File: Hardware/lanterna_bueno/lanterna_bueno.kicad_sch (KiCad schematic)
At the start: 52 parts, among them Q4 2SK4075, Q5 2SK4075

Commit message: building
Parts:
- removed C10, C7: (no value), symbol Device:C
- removed D6: (no value), symbol Diode:BAT54C
- removed JP1: (no value), symbol Jumper:SolderJumper_2_Open
- removed R8: (no value), symbol Device:R
- removed U4: (no value), symbol MCU_ST_STM32F1:STM32F103CBTx
- added U4: (no value), symbol MCU_ST_STM32F0:STM32F042K6Tx
- C1, C3, C6: value (none) -> 1uF; footprint (none) -> Capacitor_SMD:C_1206_3216Metric
- C11, C14: value (none) -> 10uF; footprint (none) -> Capacitor_SMD:C_1206_3216Metric
- C13: value 2.2uF -> (none); footprint Capacitor_SMD:C_1206_3216Metric -> (none)
- C2: value (none) -> 22nF; footprint (none) -> Capacitor_SMD:C_0603_1608Metric
- C4, C5: value (none) -> 1uF; footprint (none) -> Capacitor_SMD:CP_Elec_4x3
- C8, C9: value (none) -> 100nF; footprint (none) -> Capacitor_SMD:C_0603_1608Metric
- D2: value 1N5819 -> (none); footprint Diode_THT:D_DO-41_SOD81_P10.16mm_Horizontal -> (none)
- D3: value (none) -> LED
- DS1: value (none) -> OLED-128O064D; footprint (none) -> Display:OLED-128O064D
- J1: value (none) -> USB_B_Micro; footprint (none) -> Connector_USB:USB_Micro-B_Wuerth_629105150521
- Q1: value (none) -> BC807; footprint (none) -> Package_TO_SOT_SMD:SOT-23
- Q2, Q3: value (none) -> 2SK4075; footprint (none) -> Package_TO_SOT_SMD:TO-252-2
- R1: value (none) -> 100k; footprint (none) -> Resistor_SMD:R_0603_1608Metric
- R10: value (none) -> 0R4; footprint (none) -> Resistor_SMD:R_0603_1608Metric
- R11: value (none) -> 1K5; footprint (none) -> Resistor_SMD:R_0603_1608Metric
- R12: value (none) -> 0R; footprint (none) -> Resistor_SMD:R_0603_1608Metric
- R13, R2, R3, R9: value (none) -> 47K; footprint (none) -> Resistor_SMD:R_0603_1608Metric
- R14: value (none) -> 100K; footprint (none) -> Resistor_SMD:R_0603_1608Metric
- R15: value (none) -> 4K7; footprint (none) -> Resistor_SMD:R_0603_1608Metric
- R16: value (none) -> 390R; footprint (none) -> Resistor_SMD:R_0603_1608Metric
- R4, R5, R6, R7: value (none) -> 10R; footprint (none) -> Resistor_SMD:R_0603_1608Metric
- U1: value (none) -> RT9193-33; footprint (none) -> Package_TO_SOT_SMD:SOT-23-5
- U2, U3: value (none) -> IR2101; footprint (none) -> Package_SO:SOIC-8_3.9x4.9mm_P1.27mm
- U5: value (none) -> TP4056; footprint (none) -> Package_SO:Infineon_PG-DSO-8-43
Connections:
- net +3V3: now also U4.1 (VDD), U4.17 (VDDIO2), U4.5 (VDDA)
- net BAT_MON: now also U4.6 (PA0)
- net BUT_MENU: now also U4.28 (PB5)
- net BUT_MINUS: now also U4.26 (PB3)
- net BUT_PLUS: now also U4.27 (PB4)
- net GND: now also U4.16 (VSS), U4.32 (VSSA)
- net LCD_SCL: now also U4.3 (PF1)
- net LCD_SDA: now also U4.2 (PF0)
- net POWER_CMD: now also U4.29 (PB6)
- net PWM_LED_INFH: now also U4.14 (PB0)
- net PWM_LED_INFL: now also U4.15 (PB1)
- net PWM_LED_SUPH: now also U4.12 (PA6)
- net PWM_LED_SUPL: now also U4.13 (PA7)
- net at R9.2: now also U4.4 (NRST)
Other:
- moved on the sheet: R9

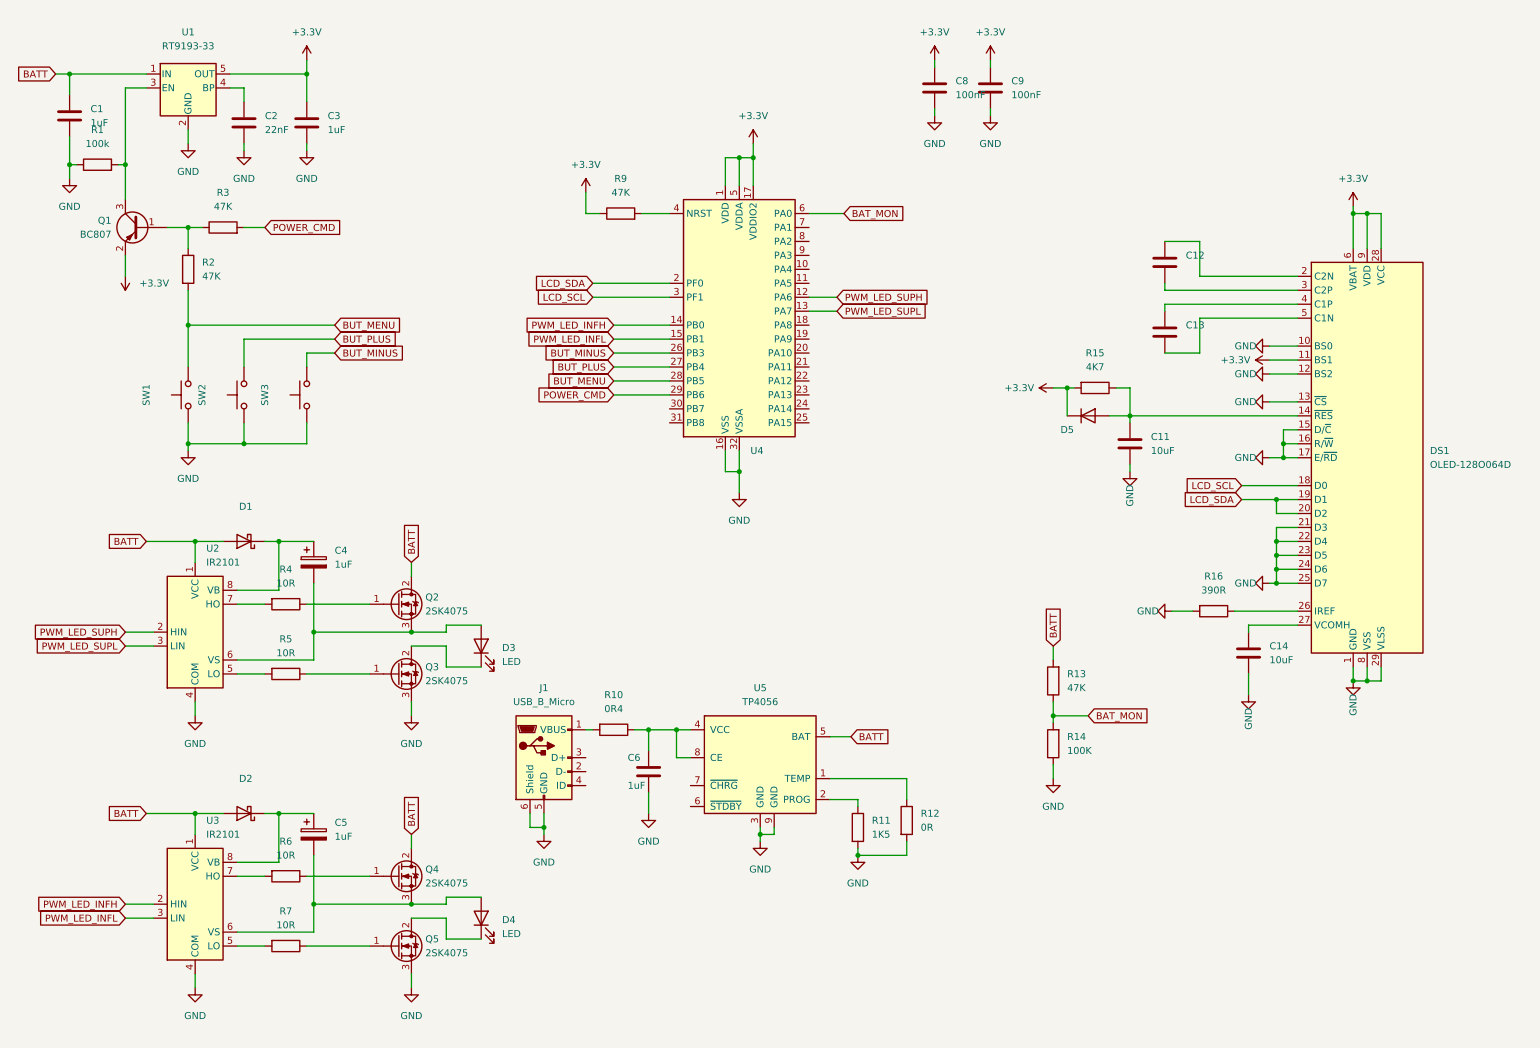
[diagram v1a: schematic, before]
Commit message: usb c
falta posicionar
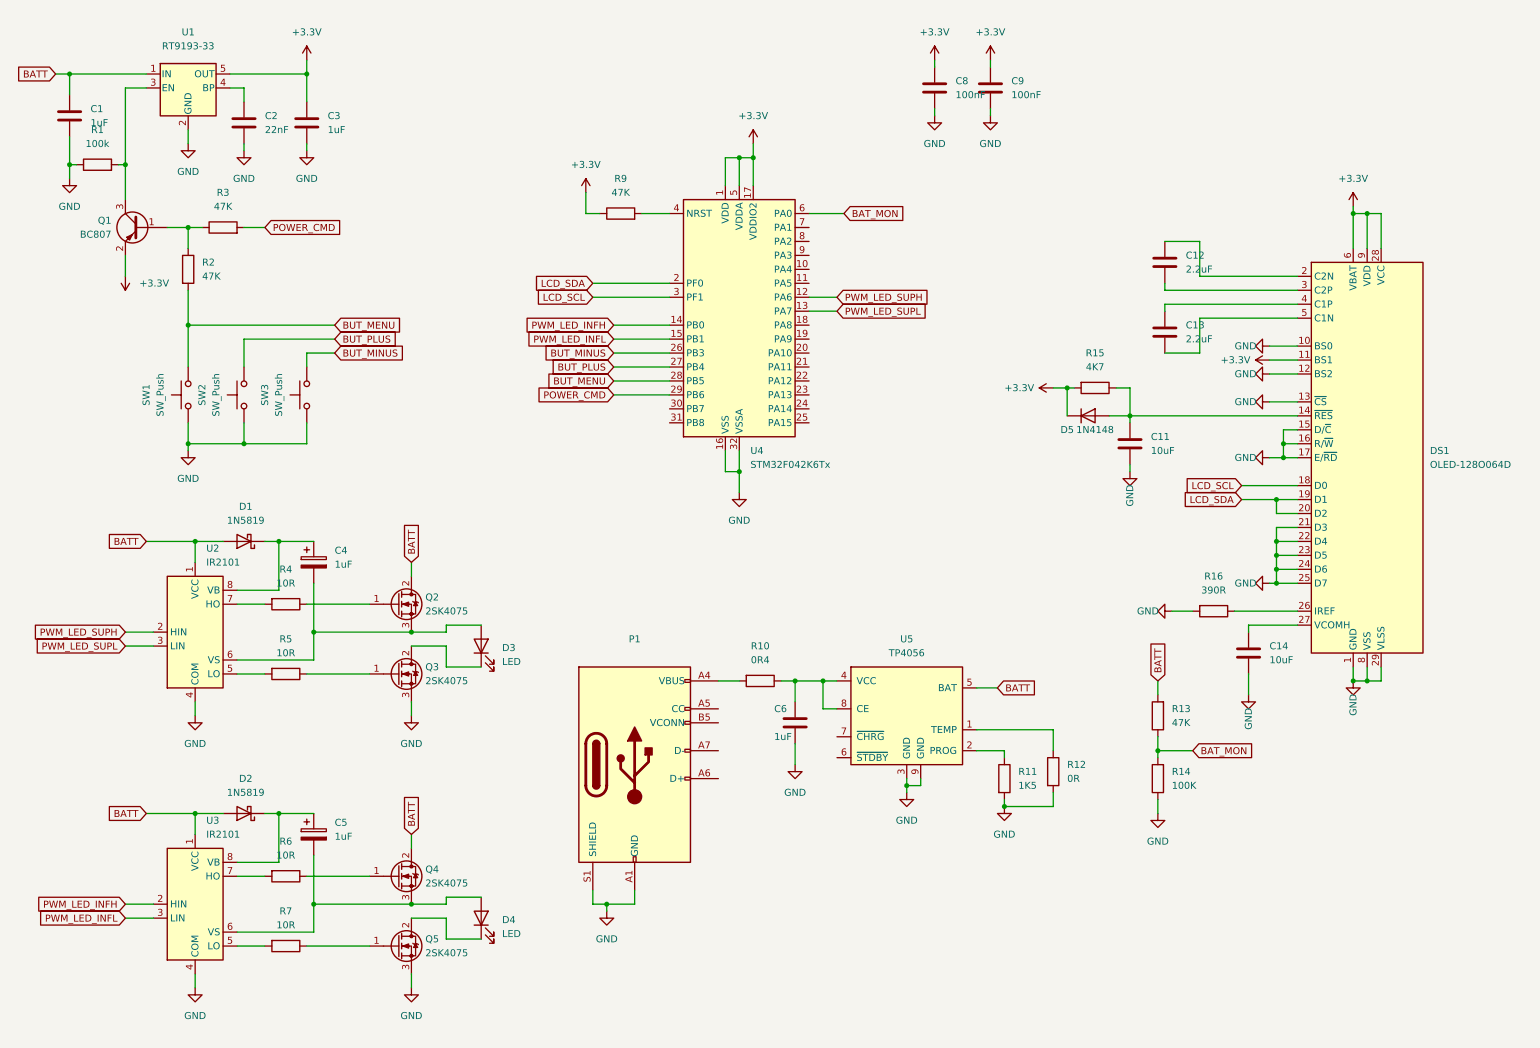
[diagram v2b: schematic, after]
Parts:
- removed J1: USB_B_Micro, Connector_USB:USB_Micro-B_Wuerth_629105150521, symbol Connector:USB_B_Micro
- added P1: (no value), symbol Connector:USB_C_Plug_USB2.0
- C12, C13: value (none) -> 2.2uF; footprint (none) -> Capacitor_SMD:C_0603_1608Metric
- D1, D2: value (none) -> 1N5819; footprint (none) -> Diode_SMD:D_SMA
- D5: value (none) -> 1N4148; footprint (none) -> Diode_SMD:D_SOD-123
- SW1, SW2, SW3: value (none) -> SW_Push; footprint (none) -> Button_Switch_SMD:SW_Push_1P1T_NO_6x6mm_H9.5mm
- U4: value (none) -> STM32F042K6Tx; footprint (none) -> Package_QFP:LQFP-32_7x7mm_P0.8mm
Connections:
- net GND: now also P1.A1 (GND), P1.A12 (GND), P1.B1 (GND), P1.B12 (GND), P1.S1 (SHIELD)
- net at R10.2: now also P1.A4 (VBUS), P1.A9 (VBUS), P1.B4 (VBUS), P1.B9 (VBUS)
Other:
- moved on the sheet: C6, R10, R11, R12, R13, R14, U5

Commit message: building pcb
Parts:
- removed D3, D4: LED, symbol Device:LED
- removed P1: (no value), symbol Connector:USB_C_Plug_USB2.0
- removed Q2, Q3, Q4, Q5: 2SK4075, Package_TO_SOT_SMD:TO-252-2, symbol Transistor_FET:2SK4075
- added J1: Conn_01x02_Male, Connector:SMD_BAT, symbol Connector:Conn_01x02_Male
- added J10, J11, J8, J9: Conn_01x03_Male, Connector:3pin 90 pcb solder, symbol Connector:Conn_01x03_Male
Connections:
- net BATT: now also J1.1 (Pin_1)
- net GND: now also J1.2 (Pin_2), J9.2 (Pin_2), J9.3 (Pin_3)
- net TRANSISTOR_1_P1_1: now reaches R4.1
- net TRANSISTOR_1_P1_1: now also J10.1 (Pin_1)
- net TRANSISTOR_1_P2_1: now reaches C4.2, U2.6 (VS)
- net TRANSISTOR_1_P2_1: now also J10.2 (Pin_2)
- net TRANSISTOR_2_P3_1: now reaches R7.1
- net TRANSISTOR_2_P3_1: now also J11.3 (Pin_3)
- net TRANSISTOR_2_P1_1: now reaches R6.1
- net TRANSISTOR_2_P1_1: now also J11.1 (Pin_1)
- net TRANSISTOR_2_P2_1: now reaches C5.2, U3.6 (VS)
- net TRANSISTOR_2_P2_1: now also J11.2 (Pin_2)
- net TRANSISTOR_1_P3_1: now reaches R5.1
- net TRANSISTOR_1_P3_1: now also J10.3 (Pin_3)
- net DM_1: now reaches U4.21 (PA11)
- net DM_1: now also J8.2 (Pin_2)
- net DP_1: now reaches U4.22 (PA12)
- net DP_1: now also J8.3 (Pin_3)
- net VBUS_1: now reaches R10.2
- net VBUS_1: now also J8.1 (Pin_1)
- new net BATT_1: J9.1 (Pin_1)
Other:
- added sheet PCB_led (PCB_led.kicad_sch)
- moved on the sheet: C11, C12, C13, C14, C6, D5, DS1, R10, R11, R12, R13, R14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
